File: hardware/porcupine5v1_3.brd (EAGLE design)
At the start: 28.5 x 29.7 mm, 45 parts, among them X1 PROGCON

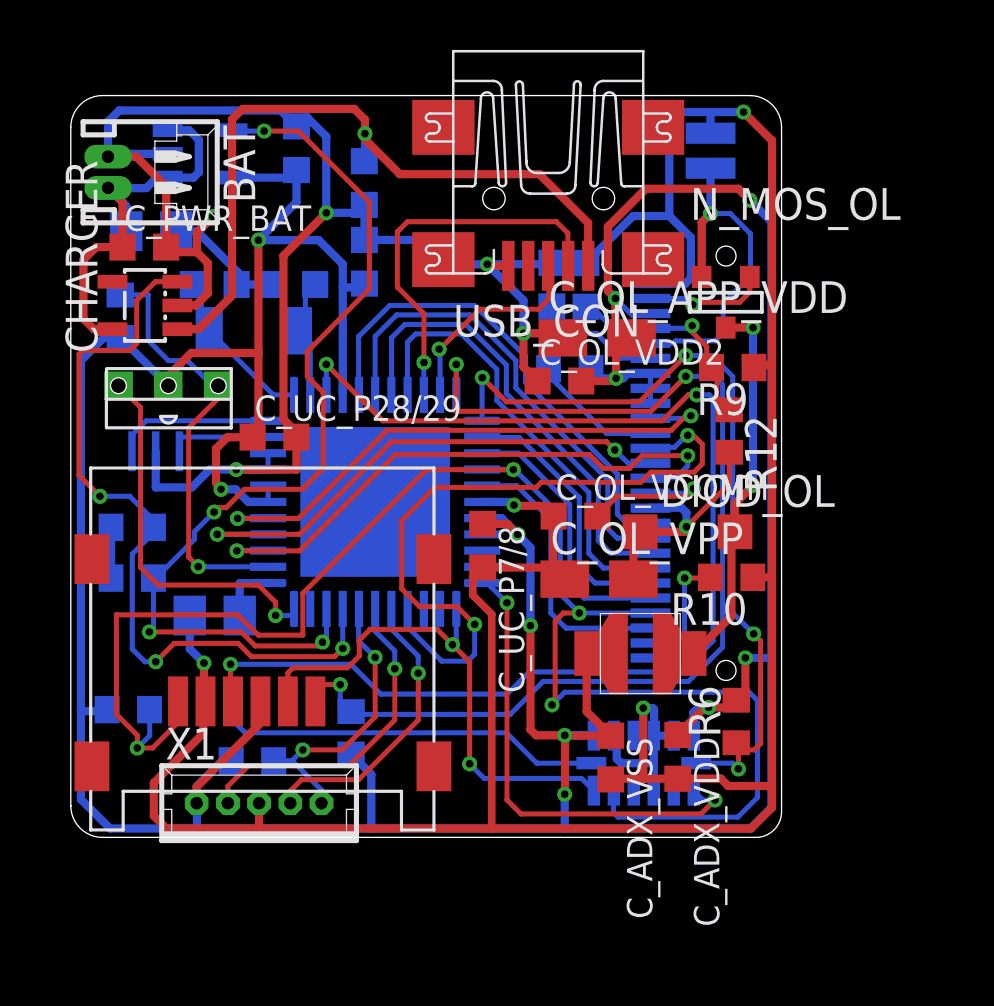
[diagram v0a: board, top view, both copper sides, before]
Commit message: OLED version update wiring
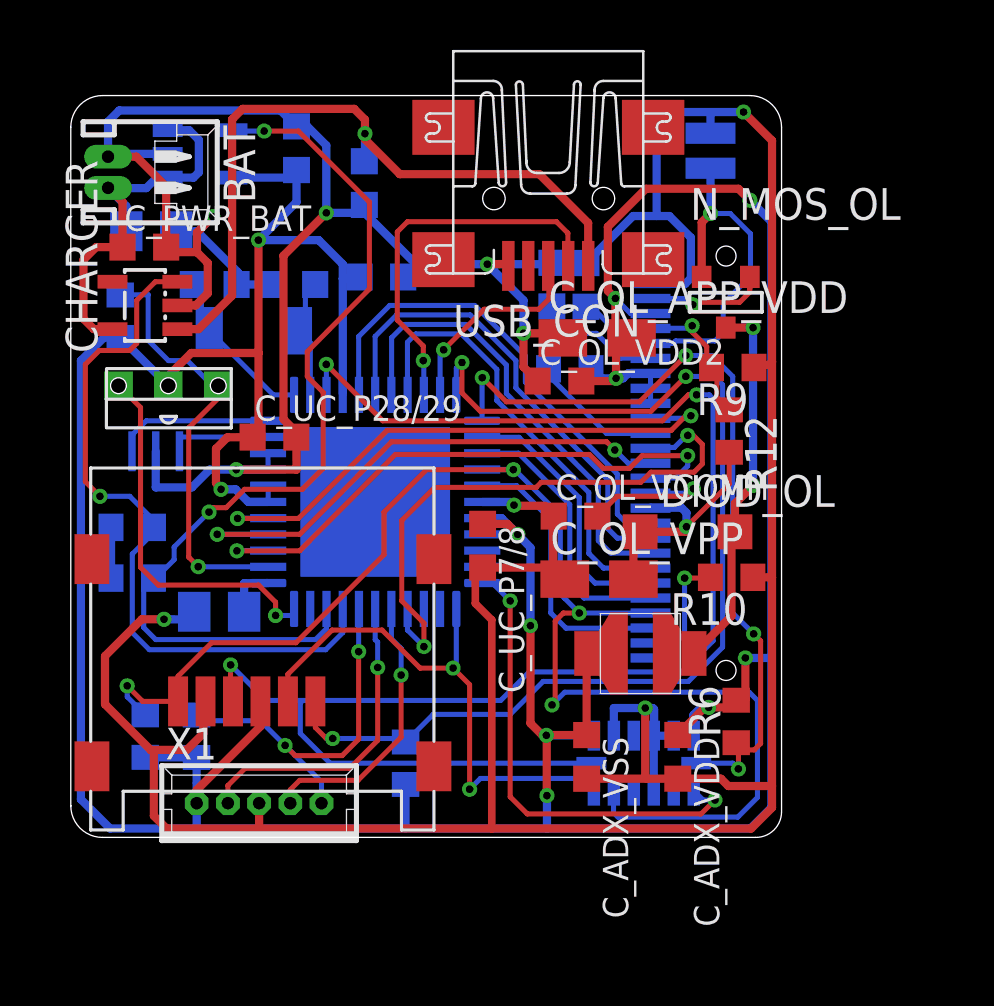
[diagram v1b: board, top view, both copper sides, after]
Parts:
- moved R4 2.50 mm to (13.4, 2.97)
- moved R1 2.45 mm to (5.04, 4.05), turned to 270 degrees
- moved R2 1.26 mm to (2.98, 4.06), turned to 270 degrees
- moved C_ADX_VSS 0.97 mm to (20.7, 3.22)
- moved C_UC_P37 0.91 mm to (12.4, 22.4), turned to 180 degrees
- moved C_UC_VDDCORE 0.23 mm to (5.94, 9.04)
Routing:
- net SDO_SPI&D6_OLED@RD6: track 66.5 -> 58.9 mm
- net GND: track 194.3 -> 200.8 mm
- net A0_OLED@RB5: track 27.7 -> 23.4 mm
- net SCLK: track 67.5 -> 63.9 mm
- net PROG_MCLR@MCLR: track 12.3 -> 15.6 mm
- net +3V3: track 179.8 -> 176.6 mm
- net POK: track 31.1 -> 28.9 mm, vias 3 -> 1
- net SDI: track 21.2 -> 22.1 mm
- net PROG_CLK@RB6: track 11.7 -> 11.1 mm
- net PWRGD: vias 4 -> 2

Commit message: OLED version updated components names and values
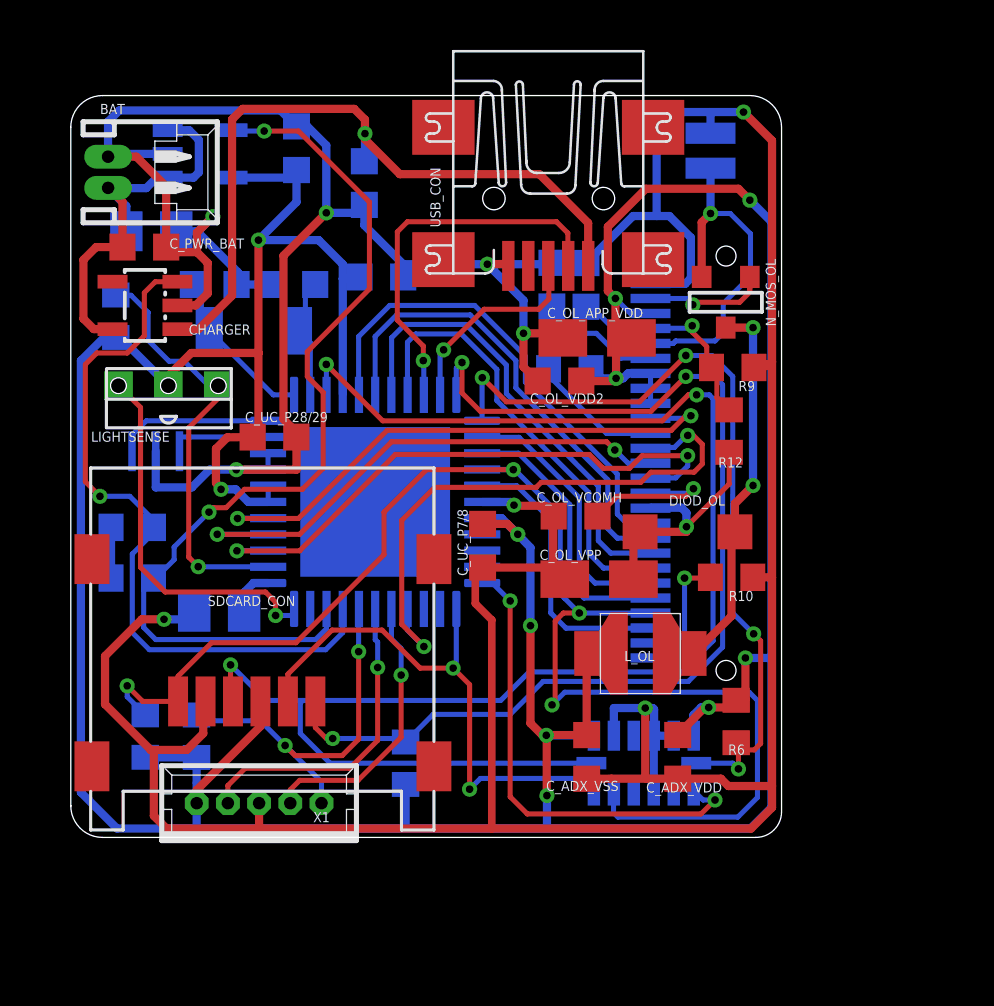
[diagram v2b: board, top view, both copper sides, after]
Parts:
- moved R7 0.18 mm to (1.80, 20.9)
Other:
- board text added: "LIGHTSENSE"
- board text added: "L_OL"
- board text added: "SDCARD_CON"

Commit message: OLED version updated wiring
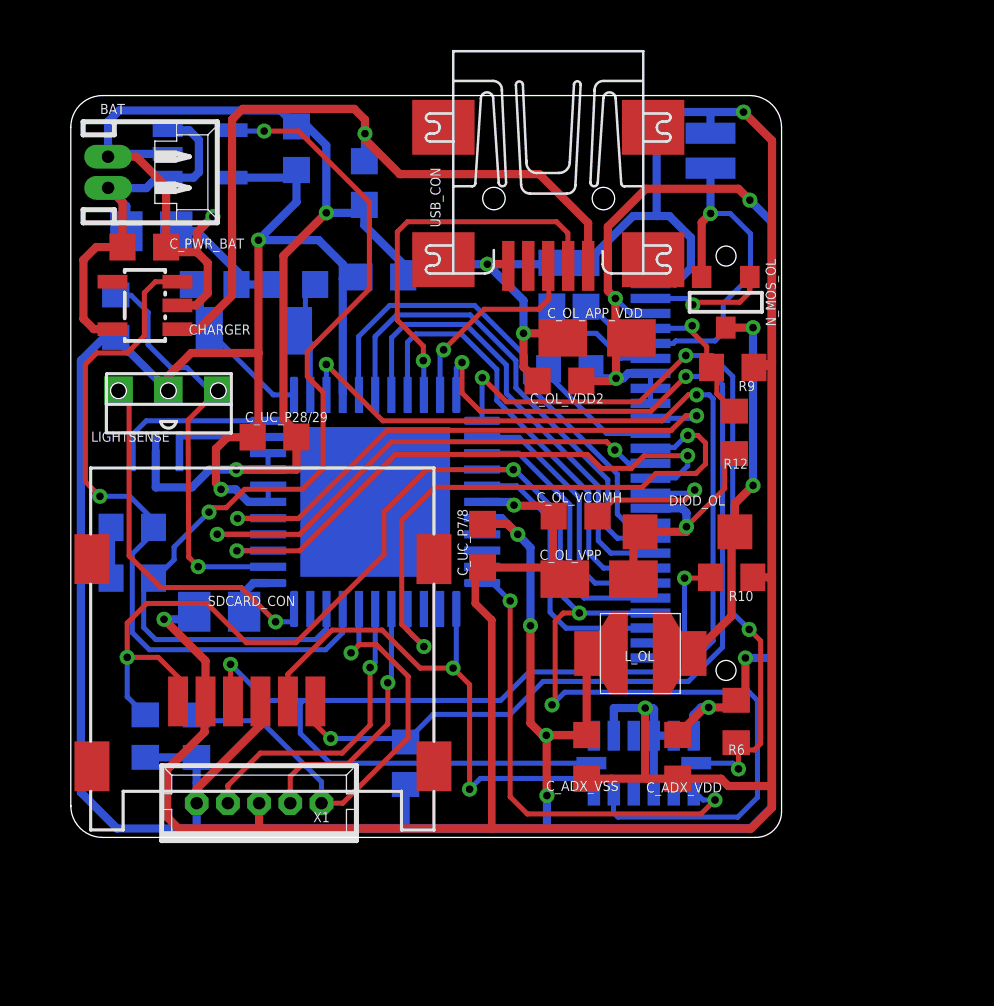
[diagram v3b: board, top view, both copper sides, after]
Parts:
- moved R12 0.21 mm to (26.6, 16.2)
- moved LIGHTSENSE 0.20 mm to (3.91, 17.9)
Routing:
- net GND: track 200.9 -> 195.0 mm
- net SDO_SPI&D6_OLED@RD6: track 58.9 -> 63.9 mm
- net PROG_MCLR@MCLR: track 15.6 -> 18.8 mm, vias 2 -> 1
- net PROG_CLK@RB6: track 11.1 -> 10.5 mm
- net PROG_DATA@RB7: track 12.8 -> 12.1 mm

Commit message: OLED version: update wiring, added layout docs
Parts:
- renumbered U$2 to SMD_CRYSTAL, U$3 to RESONATOR
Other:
- board text added: "OLED"
- board text added: "RESONATOR"
- board text added: "SMD_CRYSTAL"
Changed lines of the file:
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@@
 <grid distance="1" unitdist="mil" unit="mil" style="lines" multiple="1" display="yes" altdistance="0.025" altunitdist="inch" altunit="inch"/>
 <layers>
-<layer number="1" name="Top" color="4" fill="1" visible="yes" active="yes"/>
-<layer number="16" name="Bottom" color="1" fill="1" visible="yes" active="yes"/>
-<layer number="17" name="Pads" color="2" fill="1" visible="yes" active="yes"/>
-<layer number="18" name="Vias" color="2" fill="1" visible="yes" active="yes"/>
-<layer number="19" name="Unrouted" color="6" fill="1" visible="yes" active="yes"/>
+<layer number="1" name="Top" color="4" fill="1" visible="no" active="yes"/>
+<layer number="16" name="Bottom" color="1" fill="1" visible="no" active="yes"/>
+<layer number="17" name="Pads" color="2" fill="1" visible="no" active="yes"/>
+<layer number="18" name="Vias" color="2" fill="1" visible="no" active="yes"/>
+<layer number="19" name="Unrouted" color="6" fill="1" visible="no" active="yes"/>
 <layer number="20" name="Dimension" color="15" fill="1" visible="yes" active="yes"/>
-<layer number="21" name="tPlace" color="7" fill="1" visible="yes" active="yes"/>
+<layer number="21" name="tPlace" color="7" fill="1" visible="no" active="yes"/>
 <layer number="22" name="bPlace" color="7" fill="1" visible="yes" active="yes"/>
-<layer number="23" name="tOrigins" color="15" fill="1" visible="yes" active="yes"/>
+<layer number="23" name="tOrigins" color="15" fill="1" visible="no" active="yes"/>
 <layer number="24" name="bOrigins" color="15" fill="1" visible="yes" active="yes"/>
 <layer number="25" name="tNames" color="7" fill="1" visible="no" active="yes"/>
-<layer number="26" name="bNames" color="7" fill="1" visible="no" active="yes"/>
+<layer number="26" name="bNames" color="7" fill="1" visible="yes" active="yes"/>
 <layer number="27" name="tValues" color="7" fill="1" visible="no" active="yes"/>
 <layer number="28" name="bValues" color="7" fill="1" visible="no" active="yes"/>
@@
 <layer number="37" name="tTest" color="7" fill="1" visible="no" active="yes"/>
 <layer number="38" name="bTest" color="7" fill="1" visible="no" active="yes"/>
-<layer number="39" name="tKeepout" color="4" fill="11" visible="yes" active="yes"/>
-<layer number="40" name="bKeepout" color="1" fill="11" visible="yes" active="yes"/>
-<layer number="41" name="tRestrict" color="4" fill="10" visible="yes" active="yes"/>
-<layer number="42" name="bRestrict" color="1" fill="10" visible="yes" active="yes"/>
+<layer number="39" name="tKeepout" color="4" fill="11" visible="no" active="yes"/>
+<layer number="40" name="bKeepout" color="1" fill="11" visible="no" active="yes"/>
+<layer number="41" name="tRestrict" color="4" fill="10" visible="no" active="yes"/>
+<layer number="42" name="bRestrict" color="1" fill="10" visible="no" active="yes"/>
 <layer number="43" name="vRestrict" color="2" fill="10" visible="no" active="yes"/>
 <layer number="44" name="Drills" color="7" fill="1" visible="no" active="yes"/>
-<layer number="45" name="Holes" color="7" fill="1" visible="no" active="yes"/>
+<layer number="45" name="Holes" color="7" fill="1" visible="yes" active="yes"/>
 <layer number="46" name="Milling" color="3" fill="1" visible="no" active="yes"/>
 <layer number="47" name="Measures" color="7" fill="1" visible="no" active="yes"/>
@@
 <layer number="49" name="Reference" color="7" fill="1" visible="no" active="yes"/>
 <layer number="50" name="dxf" color="7" fill="1" visible="no" active="yes"/>
-<layer number="51" name="tDocu" color="7" fill="1" visible="yes" active="yes"/>
+<layer number="51" name="tDocu" color="7" fill="1" visible="no" active="yes"/>
 <layer number="52" name="bDocu" color="7" fill="1" visible="yes" active="yes"/>
 <layer number="53" name="tGND_GNDA" color="7" fill="9" visible="no" active="no"/>
@@
 <text x="5.4864" y="9.271" size="0.4064" layer="25">SDCARD_CON</text>
 <text x="22.1742" y="7.0612" size="0.4064" layer="25">L_OL</text>
+<text x="27.7368" y="15.9004" size="0.4064" layer="26" rot="MR270">OLED</text>
+<text x="9.4742" y="19.0246" size="0.4064" layer="26" rot="MR0">SMD_CRYSTAL</text>
+<text x="5.1054" y="14.3002" size="0.4064" layer="26" rot="MR0">RESONATOR</text>
 </plain>
 <attributes>
@@
 <attribute name="VALUE" x="1.4478" y="10.8204" size="0.4064" layer="28" rot="MR270"/>
 </element>
-<element name="U$2" library="HedgehogLib" package="SMD_CRYSTAL" value="SMD_CRYSTAL" x="7.3406" y="20.2946" smashed="yes" rot="MR0"/>
-<element name="U$3" library="jnode" package="PRQC" value="RESONATORPRQC-S" x="3.4036" y="15.4686" smashed="yes" rot="MR180">
+<element name="SMD_CRYSTAL" library="HedgehogLib" package="SMD_CRYSTAL" value="SMD_CRYSTAL" x="7.3406" y="20.2946" smashed="yes" rot="MR0"/>
+<element name="RESONATOR" library="jnode" package="PRQC" value="RESONATORPRQC-S" x="3.4036" y="15.4686" smashed="yes" rot="MR180">
 <attribute name="DIGIKEY" value="http://search.digikey.com/scripts/DkSearch/dksus.dll?Detail&amp;name=478-5420-1-ND" x="3.4036" y="15.4686" size="1.778" layer="28" rot="MR180" display="off"/>
 </element>
@@
 <via x="23.0124" y="5.1816" extent="1-16" drill="0.3048" shape="octagon"/>
 <contactref element="LDO" pad="2"/>
-<contactref element="U$3" pad="GND"/>
+<contactref element="RESONATOR" pad="GND"/>
 <wire x1="8.0404" y1="22.1488" x2="6.6408" y2="22.1488" width="0.3302" layer="16"/>
 <wire x1="6.6916" y1="22.6454" x2="6.6408" y2="22.1488" width="0.3302" layer="16"/>
@@
 <contactref element="C2_32KHZ" pad="1"/>
 <contactref element="PIC_CONTROLLER" pad="34"/>
-<contactref element="U$2" pad="P$1"/>
+<contactref element="SMD_CRYSTAL" pad="P$1"/>
 <wire x1="5.6134" y1="20.2946" x2="5.5466" y2="20.2946" width="0.3302" layer="16"/>
 <wire x1="8.9448" y1="17.7279" x2="8.1133" y2="17.7279" width="0.2032" layer="16"/>
@@
 <contactref element="C1_32KHZ" pad="1"/>
 <contactref element="PIC_CONTROLLER" pad="35"/>
-<contactref element="U$2" pad="P$2"/>
+<contactref element="SMD_CRYSTAL" pad="P$2"/>
 <wire x1="9.5948" y1="17.7269" x2="9.5948" y2="19.8184" width="0.2032" layer="16"/>
 <wire x1="9.5948" y1="19.8184" x2="9.1186" y2="20.2946" width="0.2032" layer="16"/>
@@
 <signal name="N$1">
 <contactref element="PIC_CONTROLLER" pad="33"/>
-<contactref element="U$3" pad="1"/>
+<contactref element="RESONATOR" pad="1"/>
 <wire x1="7.9103" y1="16.6894" x2="3.0242" y2="16.6894" width="0.2032" layer="16"/>
 <wire x1="3.0242" y1="16.6894" x2="2.4536" y2="16.1188" width="0.2032" layer="16"/>
@@
 </signal>
 <signal name="N$2">
-<contactref element="U$3" pad="2"/>
+<contactref element="RESONATOR" pad="2"/>
 <contactref element="PIC_CONTROLLER" pad="32"/>
 <wire x1="7.9023" y1="16.0414" x2="4.3536" y2="16.0414" width="0.2032" layer="16"/>
